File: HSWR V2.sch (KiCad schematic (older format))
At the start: 25 parts, among them J1 IO, J4 USB_B, J5 B+, J6 B-, J7 U, J8 V, J9 W

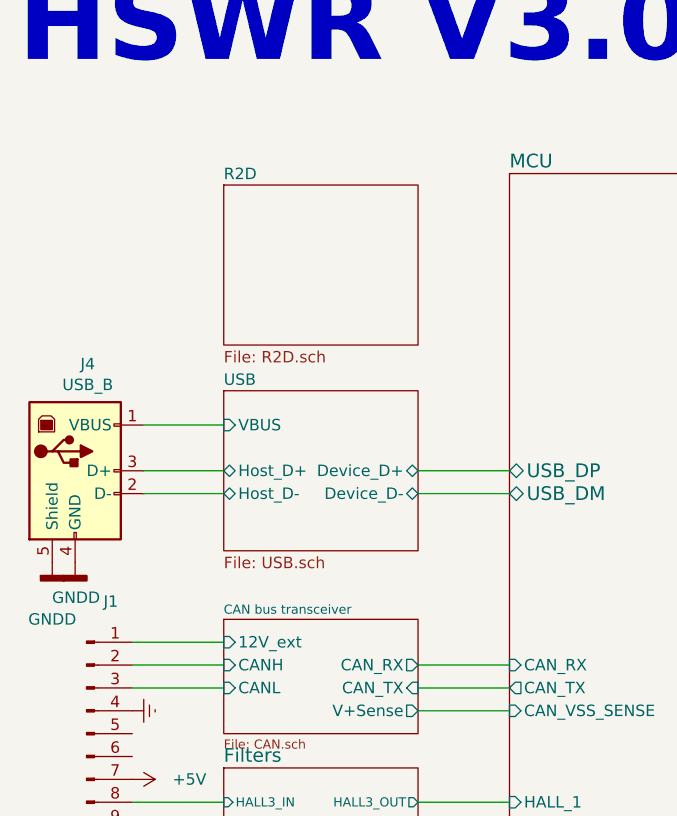
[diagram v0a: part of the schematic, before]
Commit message: - removed R2D.sch - selected PSUs - finished layout
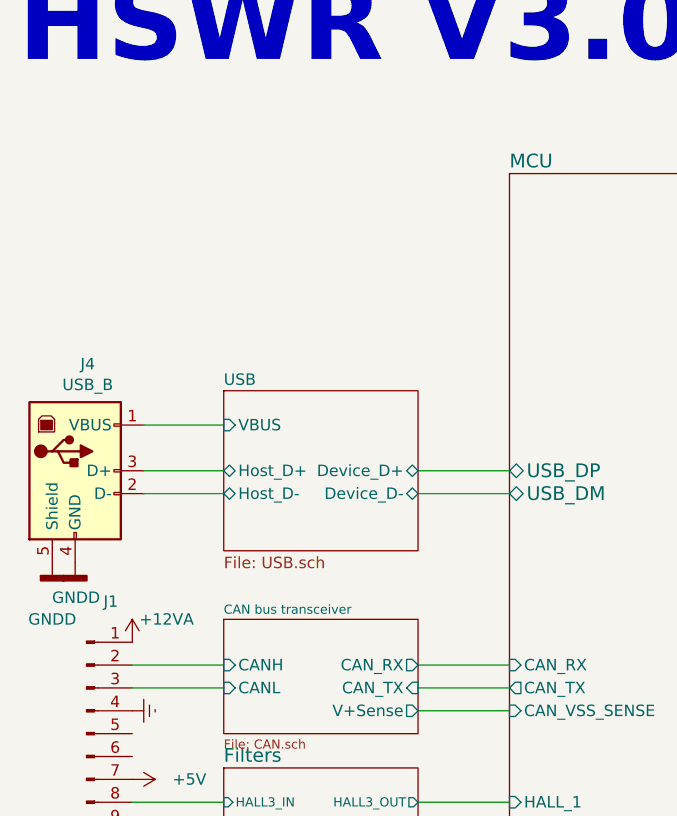
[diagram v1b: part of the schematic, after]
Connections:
- net CAN bus transceiver/12V_ext renamed +12VA
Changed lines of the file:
@@
 $Descr A4 11693 8268
 encoding utf-8
-Sheet 1 9
+Sheet 1 8
 Title "HSWR V2.0 200V 50A"
 Date "2017-02-05"
@@
 F0 "CAN bus transceiver" 40
 F1 "CAN.sch" 40
-F2 "12V_ext" I L 1700 3700 50
-F3 "CAN_RX" O R 2550 3800 50
-F4 "CAN_TX" I R 2550 3900 50
-F5 "CANH" I L 1700 3800 50
-F6 "V+Sense" O R 2550 4000 50
-F7 "CANL" I L 1700 3900 50
+F2 "CAN_RX" O R 2550 3800 50
+F3 "CAN_TX" I R 2550 3900 50
+F4 "CANH" I L 1700 3800 50
+F5 "V+Sense" O R 2550 4000 50
+F6 "CANL" I L 1700 3900 50
 $EndSheet
 Wire Wire Line
-	1700 3700 1300 3700
-Wire Wire Line
 	2950 4000 2550 4000
 Wire Wire Line
@@
 	1    0    0    -1
 $EndComp
-$Sheet
-S 1700 1700 850  700
-U 5CA305B7
-F0 "R2D" 50
-F1 "R2D.sch" 50
-$EndSheet
+$Comp
+L power:+12VA #PWR0194
+U 1 1 5C9EFA56
+P 1300 3700
+F 0 "#PWR0194" H 1300 3550 50  0001 C CNN
+F 1 "+12VA" H 1450 3800 50  0000 C CNN
+F 2 "" H 1300 3700 50  0001 C CNN
+F 3 "" H 1300 3700 50  0001 C CNN
+	1    1300 3700
+	1    0    0    -1
+$EndComp
 $EndSCHEMATC

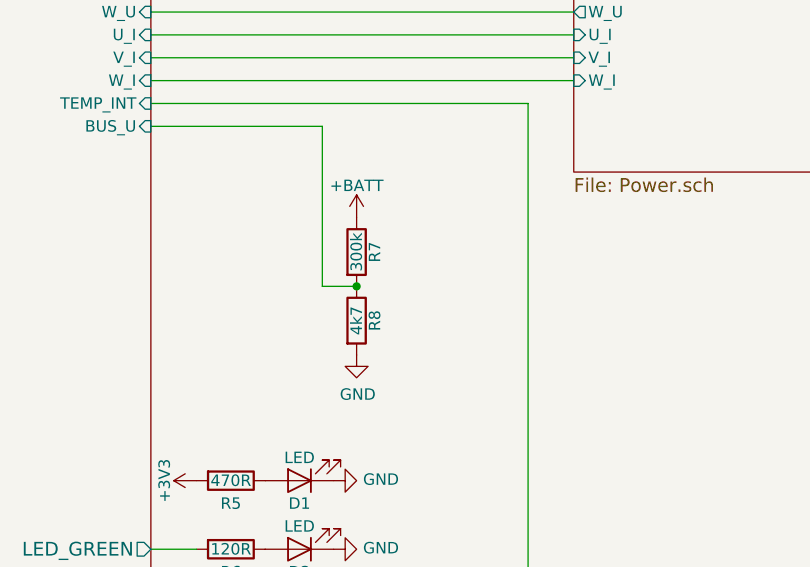
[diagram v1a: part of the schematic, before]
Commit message: - corrected current filter resistors - adapted USB footprint - added 0.1% note to dc bus voltage divider
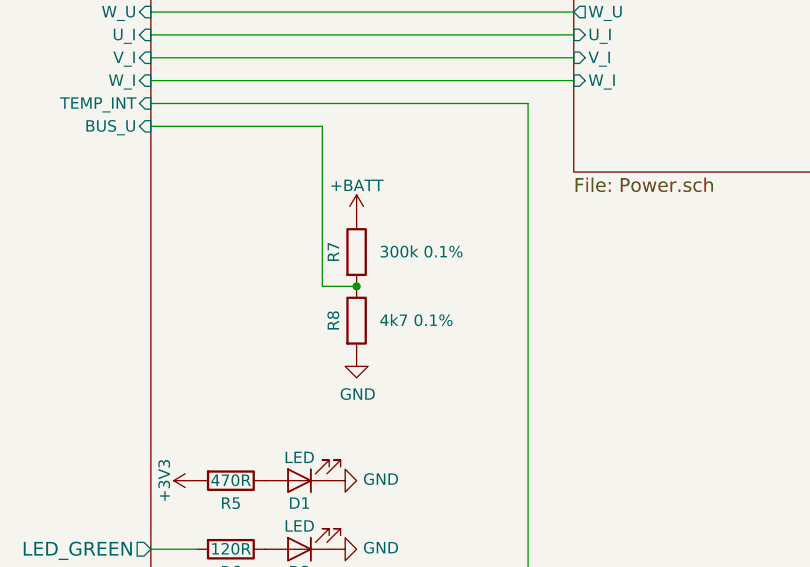
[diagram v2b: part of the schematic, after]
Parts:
- R7: value 300k -> 300k 0.1%
- R8: value 4k7 -> 4k7 0.1%
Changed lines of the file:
@@
 U 1 1 5895E69E
 P 5200 4350
-F 0 "R7" V 5280 4350 50  0000 C CNN
-F 1 "300k" V 5200 4350 50  0000 C CNN
+F 0 "R7" V 5100 4350 50  0000 C CNN
+F 1 "300k 0.1%" H 5300 4350 50  0000 L CNN
 F 2 "Resistor_SMD:R_0805_2012Metric" V 5130 4350 30  0001 C CNN
 F 3 "" H 5200 4350 30  0000 C CNN
@@
 U 1 1 5895E69F
 P 5200 4650
-F 0 "R8" V 5280 4650 50  0000 C CNN
-F 1 "4k7" V 5200 4650 50  0000 C CNN
+F 0 "R8" V 5100 4650 50  0000 C CNN
+F 1 "4k7 0.1%" H 5300 4650 50  0000 L CNN
 F 2 "Resistor_SMD:R_0805_2012Metric" V 5130 4650 30  0001 C CNN
 F 3 "" H 5200 4650 30  0000 C CNN

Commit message: - rescued schematic - added *.sch-bak to ignore - fixed bypass diode polarity - fixed PDEN being low - added 0R resistors instead of USB iso option - added caps to DCDC - added filter to VDDA
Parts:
- C2: symbol Device:C -> HSWR-V2-rescue:C-Device
- D1, D2, D3: symbol Device:LED -> HSWR-V2-rescue:LED-Device
- J1: symbol Connector:Conn_01x20_Male -> HSWR-V2-rescue:Conn_01x20_Male-Connector
- J4: symbol Connector:USB_B -> HSWR-V2-rescue:USB_B-Connector
- J5, J6, J7, J8, J9: symbol Connector:Conn_01x01_Male -> HSWR-V2-rescue:Conn_01x01_Male-Connector
- JP1: symbol Jumper:SolderJumper_3_Open -> HSWR-V2-rescue:SolderJumper_3_Open-Jumper
- JP2, JP3: symbol Jumper:SolderJumper_2_Open -> HSWR-V2-rescue:SolderJumper_2_Open-Jumper
- R1, R10, R11, R2, R3, R4, R5, R6, R7, R8, R9: symbol Device:R -> HSWR-V2-rescue:R-Device
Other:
- note added: "HSWR V3.1 200V 100A"
- note removed: "HSWR V3.0 200V 100A"

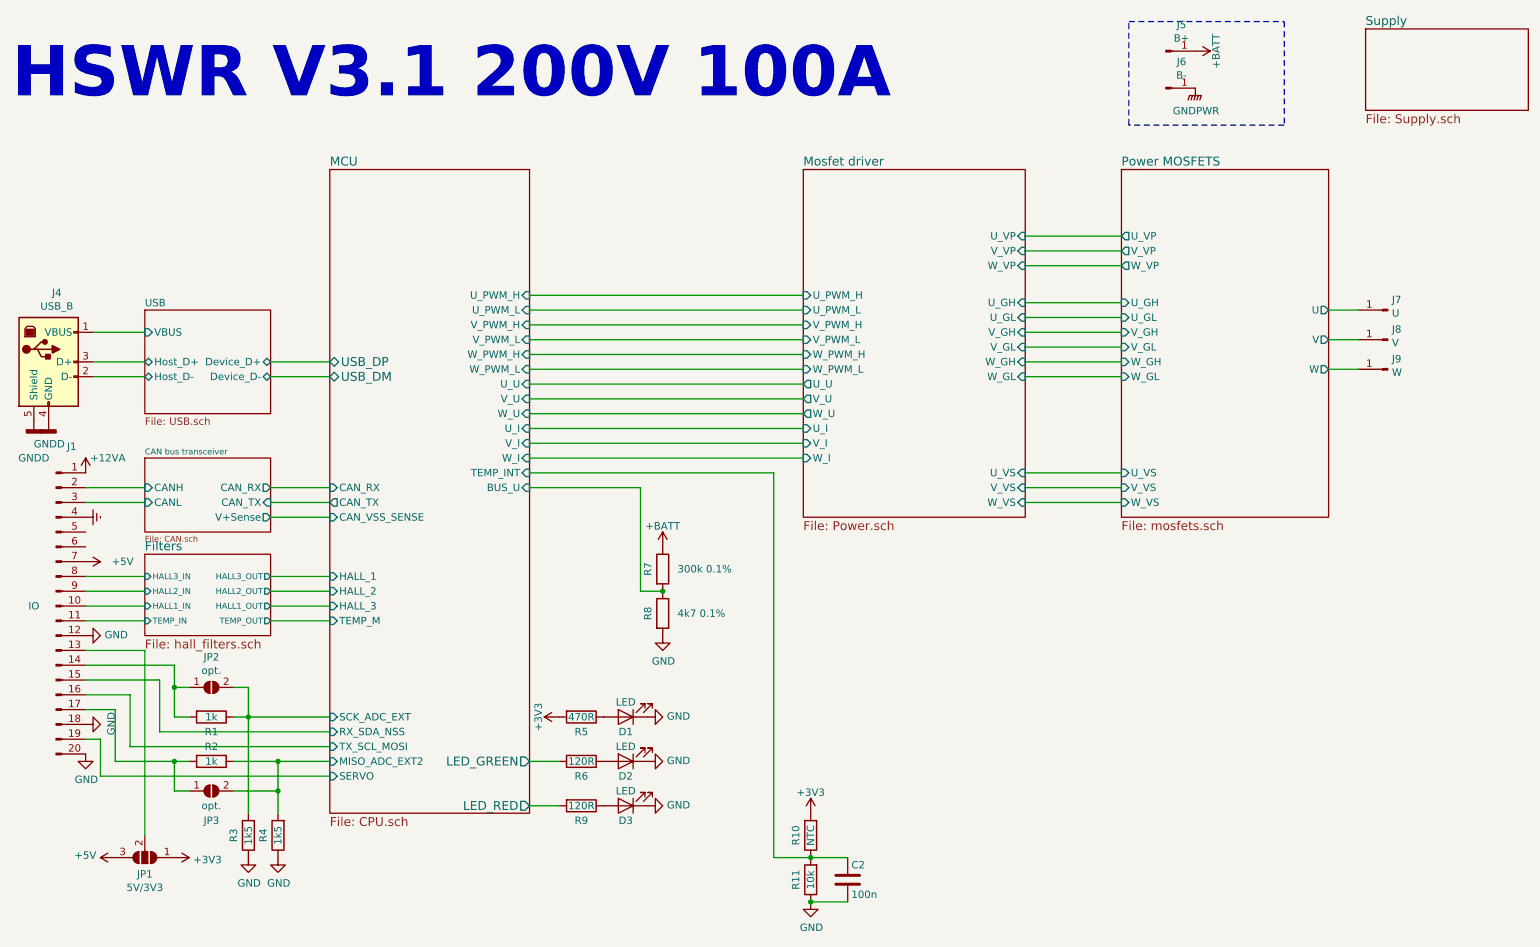
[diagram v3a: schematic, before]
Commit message: - changed CSA for Hall effect sensors - updated power stage layout
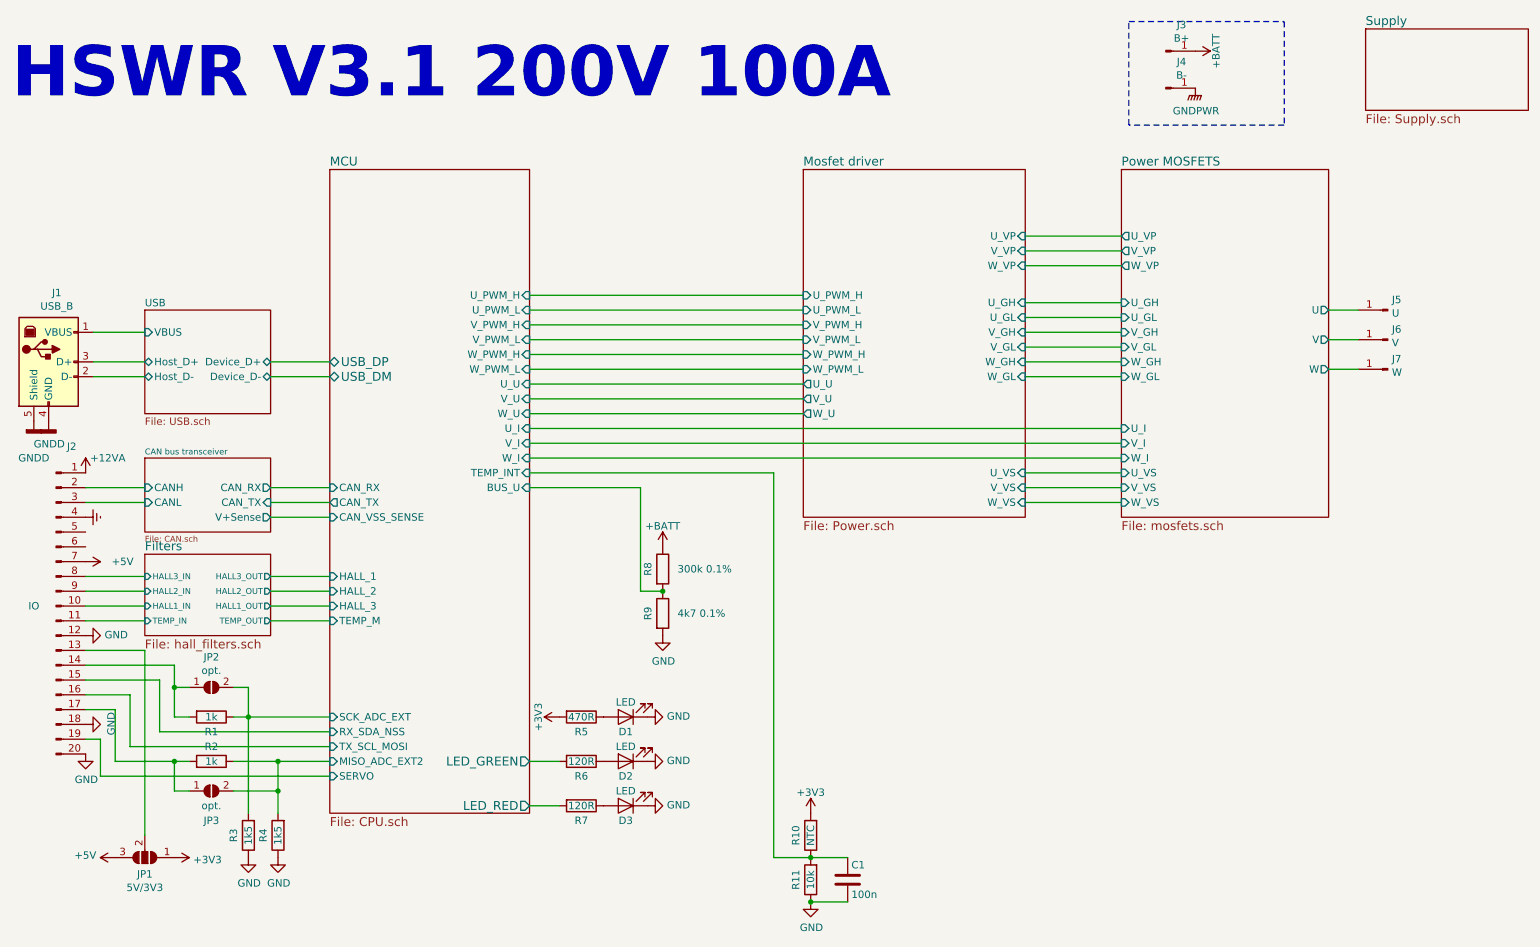
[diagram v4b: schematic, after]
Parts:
- renumbered C2 to C1, J4 to J1, J1 to J2, J5 to J3, J6 to J4, J7 to J5, J8 to J6, J9 to J7, R9 to R7, R7 to R8, R8 to R9
